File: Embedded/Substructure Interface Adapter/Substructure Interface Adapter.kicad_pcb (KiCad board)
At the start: 2 copper layers, 15.5 x 20 mm, 3 parts, among them J1 Substructure Power, J2 Pogo Pins, U1 Substructure

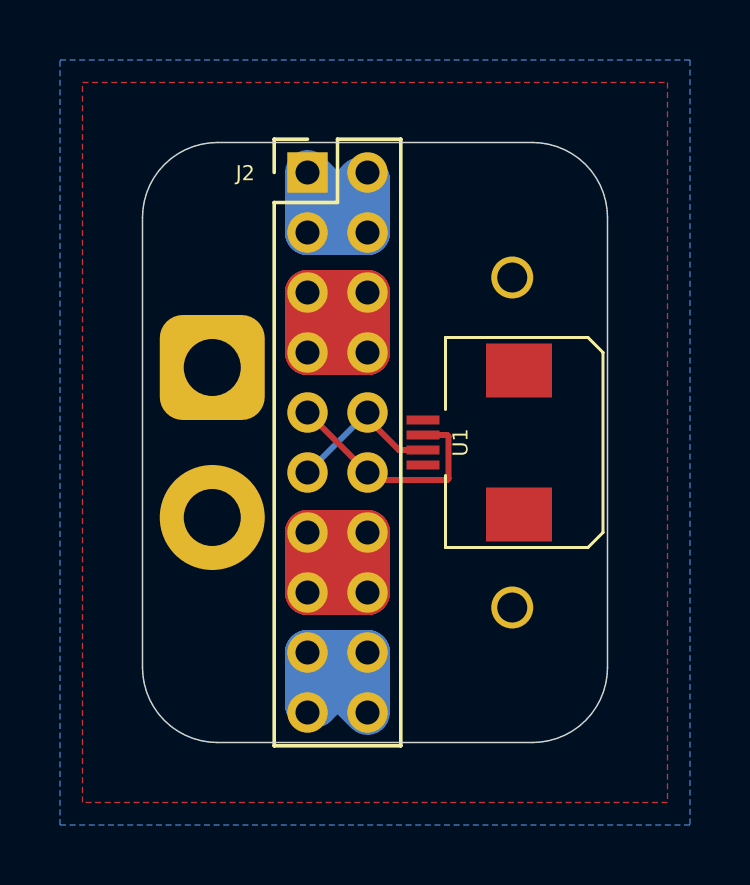
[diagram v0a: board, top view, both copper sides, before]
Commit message: Modified UART Pins & Added Silkscreen Data
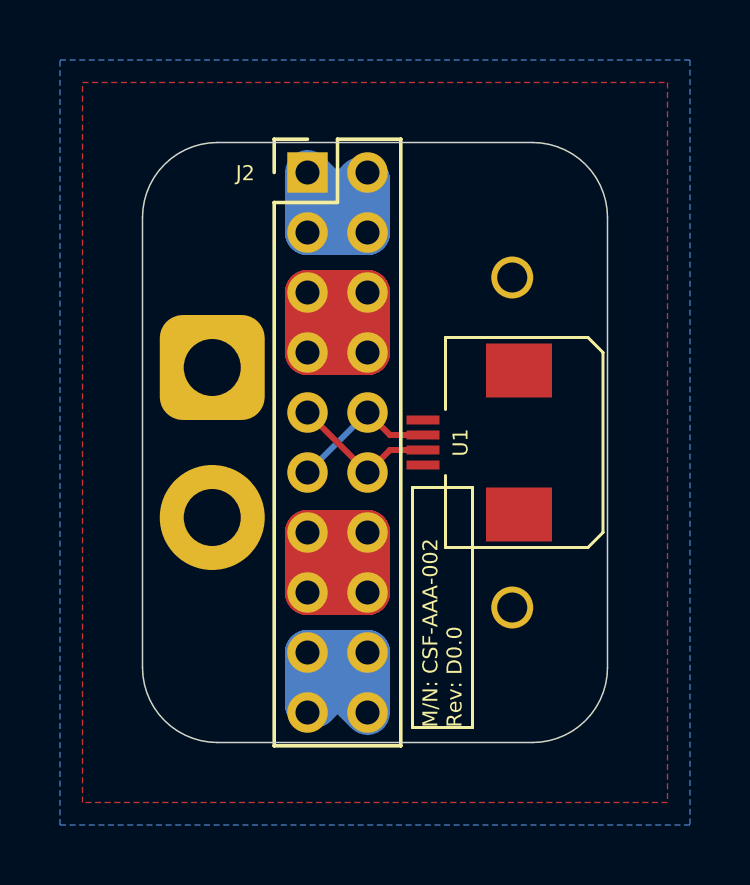
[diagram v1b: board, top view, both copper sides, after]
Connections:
- U1 pad 2: Power UART TX -> Power UART RX
- U1 pad 3: Power UART RX -> Power UART TX
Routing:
- net Power UART RX: track 7.93 -> 5.34 mm
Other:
- board text added: "M/N: CSF-AAA-002 Rev: D0.0"
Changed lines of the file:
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@@
 			(size 0.3 1.1)
 			(layers "F.Cu" "F.Mask" "F.Paste")
-			(net 3 "Power UART TX")
+			(net 4 "Power UART RX")
 			(pintype "input")
 			(thermal_bridge_angle 45)
@@
 			(size 0.3 1.1)
 			(layers "F.Cu" "F.Mask" "F.Paste")
-			(net 4 "Power UART RX")
+			(net 3 "Power UART TX")
 			(pintype "input")
 			(thermal_bridge_angle 45)
@@
 		)
 		(property "Datasheet" ""
-			(at 0 0 -90)
+			(at 0 0 270)
 			(unlocked yes)
 			(layer "B.Fab")
@@
 		)
 		(property "Description" "Generic connector, single row, 01x02, script generated"
-			(at 0 0 -90)
+			(at 0 0 270)
 			(unlocked yes)
 			(layer "B.Fab")
@@
 		)
 	)
+	(gr_rect
+		(start 102.5 61.5)
+		(end 104.5 69.5)
+		(stroke
+			(width 0.1)
+			(type default)
+		)
+		(fill no)
+		(layer "F.SilkS")
+	)
 	(gr_line
 		(start 109 67.5)
@@
 		(layer "Edge.Cuts")
 	)
+	(gr_text "M/N: CSF-AAA-002\nRev: D0.0"
+		(at 103.5 69.5 90)
+		(layer "F.SilkS")
+		(effects
+			(font
+				(size 0.5 0.5)
+				(thickness 0.1)
+			)
+			(justify left)
+		)
+	)
 	(segment
 		(start 99 65)
@@
 	)
 	(segment
-		(start 102.85 60.25)
-		(end 102.048001 60.25)
+		(start 101.75 59.75)
+		(end 101 59)
 		(width 0.2)
 		(layer "F.Cu")
@@
 	)
 	(segment
-		(start 102.048001 60.25)
-		(end 101 59.201999)
+		(start 102.850001 59.75)
+		(end 101.75 59.75)
 		(width 0.2)
 		(layer "F.Cu")
@@
 	)
 	(segment
-		(start 102.850001 59.75)
-		(end 103.652 59.75)
-		(width 0.2)
-		(layer "F.Cu")
-		(net 4)
-	)
-	(segment
-		(start 103.701 59.799)
-		(end 103.701 61.201)
-		(width 0.2)
-		(layer "F.Cu")
-		(net 4)
-	)
-	(segment
-		(start 103.652 61.25)
-		(end 101.25 61.25)
-		(width 0.2)
-		(layer "F.Cu")
-		(net 4)
-	)
-	(segment
 		(start 101.25 61.25)
 		(end 101 61)
@@
 	)
 	(segment
+		(start 101.75 60.25)
+		(end 101 61)
+		(width 0.2)
+		(layer "F.Cu")
+		(net 4)
+	)
+	(segment
 		(start 101 61)
 		(end 99 59)
@@
 	)
 	(segment
-		(start 103.701 61.201)
-		(end 103.652 61.25)
+		(start 102.85 60.25)
+		(end 101.75 60.25)
 		(width 0.2)
 		(layer "F.Cu")
-		(net 4)
-	)
-	(segment
-		(start 103.652 59.75)
-		(end 103.701 59.799)
-		(width 0.2)
-		(layer "F.Cu")
